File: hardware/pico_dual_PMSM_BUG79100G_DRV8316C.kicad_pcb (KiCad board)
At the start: 4 copper layers, 55 x 60 mm, 68 parts, among them IC1 BU79100G-LATR, IC2 BU79100G-LATR, IC3 BU79100G-LATR, IC4 BU79100G-LATR, IC5 THVD2450DRBR, J10 Conn_01x06, J11 Conn_01x06, J12 Conn_01x02_Pin, J2 Conn_01x02, U1 DRV8316CRRGFR, U3 DRV8316CRRGFR

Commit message: update pcb
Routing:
- net GND: vias 103 -> 104
- net (no net): vias 1 -> 0
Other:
- board text added: "LAAS CNRS tflayols 2026 OSOH"
- board text added: "M0"
- board text added: "M1"
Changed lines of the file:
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@@
 		(tags "capacitor")
 		(property "Reference" "C6"
-			(at 0 -1.16 0)
+			(at 2.05 0.05 0)
 			(layer "F.SilkS")
 			(effects
@@
 		(tags "capacitor")
 		(property "Reference" "C16"
-			(at 0 -1.16 0)
+			(at -2.4 -0.05 0)
 			(layer "F.SilkS")
 			(effects
@@
 		(tags "Integrated Circuit")
 		(property "Reference" "IC2"
-			(at 0 0 90)
+			(at 0 3.05 180)
 			(layer "F.SilkS")
 			(effects
@@
 		(tags "capacitor")
 		(property "Reference" "C8"
-			(at 0 -2.65 90)
+			(at 4.3 -0.05 90)
 			(layer "F.SilkS")
 			(effects
@@
 		(tags "resistor")
 		(property "Reference" "R20"
-			(at 0 -1.17 0)
+			(at -2.5 -0.3 0)
 			(layer "F.SilkS")
 			(effects
@@
 		(tags "capacitor")
 		(property "Reference" "C11"
-			(at 0 -1.16 0)
+			(at 2.45 0.05 0)
 			(layer "F.SilkS")
 			(effects
@@
 		(tags "Integrated Circuit")
 		(property "Reference" "IC1"
-			(at 0 0 90)
+			(at -0.1 -2.65 270)
 			(layer "F.SilkS")
 			(effects
@@
 		(tags "capacitor")
 		(property "Reference" "C5"
-			(at 0 -1.43 0)
+			(at 2.4 -0.05 0)
 			(layer "F.SilkS")
 			(effects
@@
 		(tags "capacitor")
 		(property "Reference" "C14"
-			(at 0 -1.68 0)
+			(at -0.28 -1.55 0)
 			(layer "F.SilkS")
 			(effects
@@
 		(tags "resistor")
 		(property "Reference" "R21"
-			(at 0 -1.17 0)
+			(at -2.5 -0.55 0)
 			(layer "F.SilkS")
 			(effects
@@
 			(at 0 -3.45 0)
 			(layer "F.SilkS")
+			(hide yes)
 			(effects
 				(font
@@
 		(tags "module usb pcb antenna")
 		(property "Reference" "A1"
-			(at 11.7475 24.765 270)
+			(at 6.2 -20.5375 0)
 			(unlocked yes)
 			(layer "F.SilkS")
@@
 			(at 0 -3.3 0)
 			(layer "F.SilkS")
+			(hide yes)
 			(effects
 				(font
@@
 		(tags "Integrated Circuit")
 		(property "Reference" "IC3"
-			(at 0 0 90)
+			(at 0 -2.97 180)
 			(layer "F.SilkS")
 			(effects
@@
 		(tags "resistor")
 		(property "Reference" "R14"
-			(at 0 -1.17 0)
+			(at -2.27 -0.2 0)
 			(layer "F.SilkS")
 			(effects
@@
 		(tags "resistor")
 		(property "Reference" "R13"
-			(at 0 -1.17 0)
+			(at -2.58 0.05 0)
 			(layer "F.SilkS")
 			(effects
@@
 		(tags "resistor")
 		(property "Reference" "R22"
-			(at 0 -1.17 90)
+			(at 0 -2.1 0)
 			(layer "F.SilkS")
 			(effects
@@
 		(tags "resistor")
 		(property "Reference" "R12"
-			(at 0 -1.17 0)
+			(at 0 -2.05 0)
 			(layer "F.SilkS")
 			(effects
@@
 		(tags "capacitor")
 		(property "Reference" "C21"
-			(at 0 -1.16 0)
+			(at 2.2 0.15 0)
 			(layer "F.SilkS")
 			(effects
@@
 		(tags "capacitor")
 		(property "Reference" "C12"
-			(at 0 -1.16 0)
+			(at 0.47 -1.05 0)
 			(layer "F.SilkS")
 			(effects
@@
 		(tags "resistor")
 		(property "Reference" "R23"
-			(at 0 -1.17 90)
+			(at 0 -2.1 180)
 			(layer "F.SilkS")
 			(effects
@@
 		(tags "capacitor")
 		(property "Reference" "C7"
-			(at 0 -1.16 0)
+			(at -0.13 2.5 0)
 			(layer "F.SilkS")
 			(effects
@@
 		(tags "capacitor")
 		(property "Reference" "C4"
-			(at 0 -1.16 0)
+			(at 0 -1.05 0)
 			(layer "F.SilkS")
 			(effects
@@
 		(tags "capacitor")
 		(property "Reference" "C18"
-			(at 0 -1.16 0)
+			(at -2.58 0.2 0)
 			(layer "F.SilkS")
 			(effects
@@
 		(tags "resistor")
 		(property "Reference" "R15"
-			(at 0 -1.17 0)
+			(at -2.5 -0.05 0)
 			(layer "F.SilkS")
 			(effects
@@
 		(tags "resistor")
 		(property "Reference" "R24"
-			(at 0 -1.17 0)
+			(at 0.1 1.05 0)
 			(layer "F.SilkS")
 			(effects
@@
 			(at 0 -3.45 0)
 			(layer "F.SilkS")
+			(hide yes)
 			(effects
 				(font
@@
 		(tags "resistor")
 		(property "Reference" "R19"
-			(at 0 -1.17 0)
+			(at -2.5 0.2 0)
 			(layer "F.SilkS")
 			(effects
@@
 		(tags "Integrated Circuit")
 		(property "Reference" "IC5"
-			(at 0 0 0)
+			(at -0.35 2.3 0)
 			(layer "F.SilkS")
 			(effects
@@
 		(tags "resistor")
 		(property "Reference" "R18"
-			(at 0 -1.17 0)
+			(at 2.3 0.1 0)
 			(layer "F.SilkS")
 			(effects
@@
 		(tags "resistor")
 		(property "Reference" "R26"
-			(at 0 -1.17 0)
+			(at -0.7 -0.95 0)
 			(layer "F.SilkS")
 			(effects
@@
 		(tags "capacitor")
 		(property "Reference" "C3"
-			(at 0 -1.16 0)
+			(at 0.13 -4.85 0)
 			(layer "F.SilkS")
 			(effects
@@
 			(at 0 -3.3 0)
 			(layer "F.SilkS")
+			(hide yes)
 			(effects
 				(font
@@
 		(tags "resistor")
 		(property "Reference" "R17"
-			(at 0 -1.17 0)
+			(at 0.23 -3.65 0)
 			(layer "F.SilkS")
 			(effects
@@
 		(tags "Integrated Circuit")
 		(property "Reference" "IC4"
-			(at 0 0 90)
+			(at -0.1 3.23 180)
 			(layer "F.SilkS")
 			(effects
@@
 		(tags "capacitor")
 		(property "Reference" "C20"
-			(at 0 -1.16 0)
+			(at 0.05 1.1 0)
 			(layer "F.SilkS")
 			(effects
@@
 		(tags "capacitor")
 		(property "Reference" "C25"
-			(at 0 -1.16 0)
+			(at -1.55 -1.16 0)
 			(layer "F.SilkS")
 			(effects
@@
 		(tags "connector Hirose DF13 vertical")
 		(property "Reference" "J12"
-			(at 0.62 -3.4 0)
+			(at 0.975 -3.4 0)
 			(layer "F.SilkS")
 			(effects
@@
 		(tags "capacitor")
 		(property "Reference" "C17"
-			(at 0 -1.16 0)
+			(at 0 -1.8 0)
 			(layer "F.SilkS")
 			(effects
@@
 		(tags "resistor")
 		(property "Reference" "R10"
-			(at 0 -1.17 0)
+			(at 0.05 -1.8 0)
 			(layer "F.SilkS")
 			(effects
@@
 		(tags "resistor")
 		(property "Reference" "R27"
-			(at 0 -1.17 0)
+			(at -0.05 0.8 0)
 			(layer "F.SilkS")
 			(effects
@@
 		(tags "capacitor")
 		(property "Reference" "C2"
-			(at 0 -2.65 90)
+			(at 3.58 0.29 180)
 			(layer "F.SilkS")
 			(effects
@@
 		(tags "resistor")
 		(property "Reference" "R16"
-			(at 0 -1.17 0)
+			(at -2.45 -0.2 0)
 			(layer "F.SilkS")
 			(effects
@@
 		(tags "resistor")
 		(property "Reference" "R11"
-			(at 0 -1.17 0)
+			(at -2.4 -0.2 0)
 			(layer "F.SilkS")
 			(effects
@@
 		(tags "capacitor")
 		(property "Reference" "C22"
-			(at 0 -1.68 0)
+			(at -3.1 0.2 0)
 			(layer "F.SilkS")
 			(effects
@@
 		(tags "resistor")
 		(property "Reference" "R25"
-			(at 0 -1.17 0)
+			(at -0.2 -0.95 0)
 			(layer "F.SilkS")
 			(effects
@@
 		(tags "capacitor")
 		(property "Reference" "C15"
-			(at 0 -1.16 0)
+			(at 0.05 -1.8 0)
 			(layer "F.SilkS")
 			(effects
@@
 		(tags "capacitor")
 		(property "Reference" "C1"
-			(at 0 -1.16 0)
+			(at 0.15 -1.05 0)
 			(layer "F.SilkS")
 			(effects
@@
 			(at 0 2.8 0)
 			(layer "B.SilkS")
+			(hide yes)
 			(effects
 				(font
@@
 			(at 0 2.8 0)
 			(layer "B.SilkS")
+			(hide yes)
 			(effects
 				(font
@@
 			(at 0 2.8 0)
 			(layer "B.SilkS")
+			(hide yes)
 			(effects
 				(font
@@
 			(at 0 2.8 0)
 			(layer "B.SilkS")
+			(hide yes)
 			(effects
 				(font
@@
 			(at 0 2.8 0)
 			(layer "B.SilkS")
+			(hide yes)
 			(effects
 				(font
@@
 			(at 0 2.8 0)
 			(layer "B.SilkS")
+			(hide yes)
 			(effects
 				(font
@@
 		)
 	)
+	(gr_text "M1"
+		(at 75 128 0)
+		(layer "B.SilkS")
+		(effects
+			(font
+				(size 1 1)
+				(thickness 0.1)
+			)
+			(justify left bottom mirror)
+		)
+	)
+	(gr_text "M0"
+		(at 89 128 0)
+		(layer "B.SilkS")
+		(effects
+			(font
+				(size 1 1)
+				(thickness 0.1)
+			)
+			(justify left bottom mirror)
+		)
+	)
+	(gr_text "LAAS CNRS tflayols \n2026 OSOH\n"
+		(at 110 165 0)
+		(layer "B.SilkS")
+		(effects
+			(font
+				(size 3 3)
+				(thickness 0.3)
+			)
+			(justify left bottom mirror)
+		)
+	)
 	(gr_text "U1"
 		(at 74.07 135.5 180)
@@
 		(net "")
 	)
-	(via
-		(at 77.39 131.46)
-		(size 0.6)
-		(drill 0.3)
-		(layers "F.Cu" "B.Cu")
-		(net "")
-	)
 	(segment
 		(start 76.475974 132.822033)
@@
 		(net "GND")
 	)
+	(via
+		(at 77.25 131.5)
+		(size 0.6)
+		(drill 0.3)
+		(layers "F.Cu" "B.Cu")
+		(net "GND")
+	)

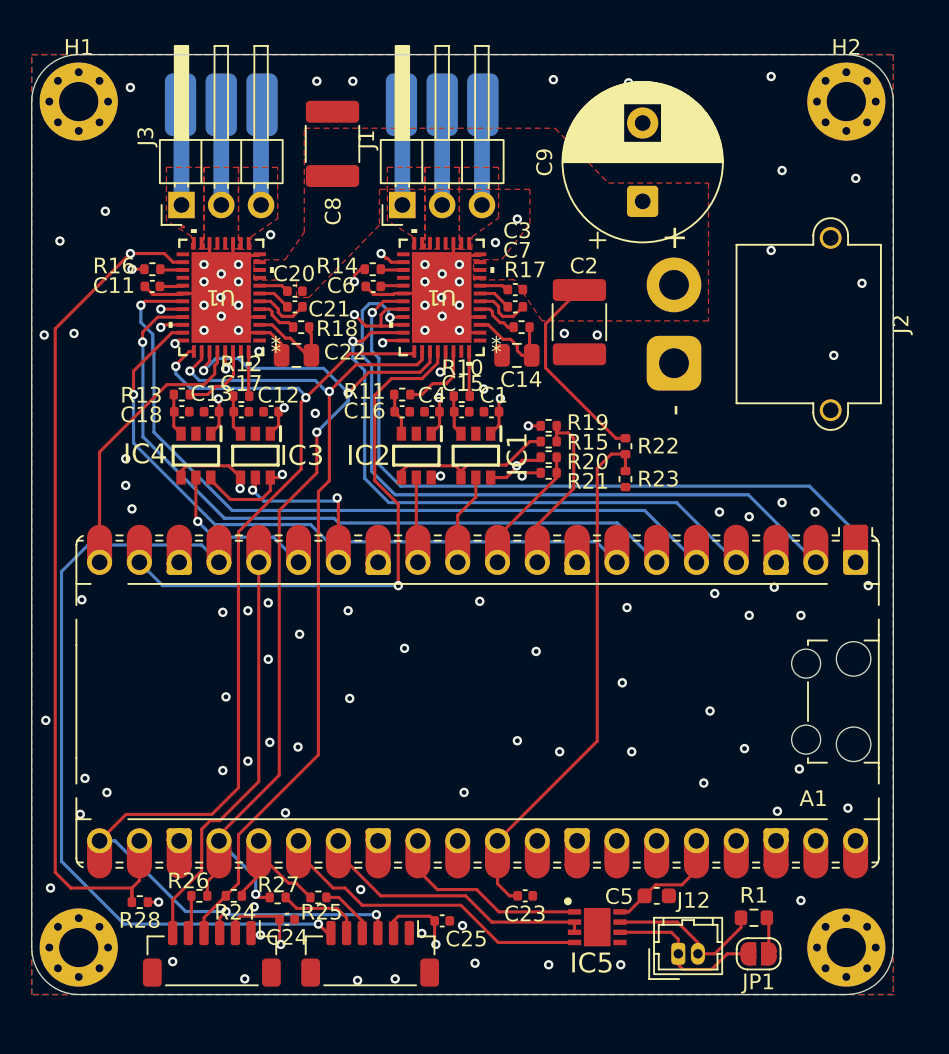
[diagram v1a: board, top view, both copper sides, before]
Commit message: add board diag at boot (press '?' at boot to test)
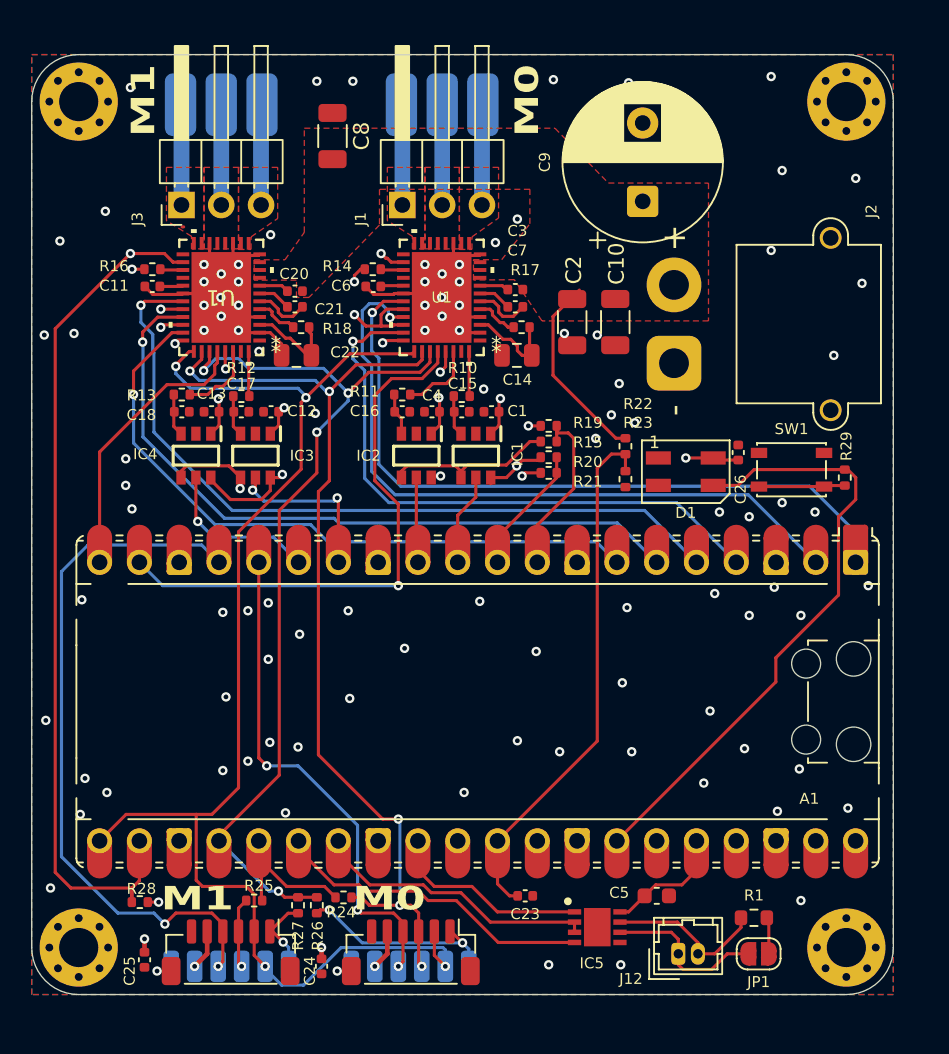
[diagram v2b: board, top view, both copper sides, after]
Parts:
- added C10: 1uF 50V, Capacitor_SMD:C_1206_3216Metric, F.Cu at (99.2, 137.1)
- added C26: 100n, Capacitor_SMD:C_0402_1005Metric, F.Cu at (107.1, 145.4)
- added D1: SK6812MINI, LED_SMD:LED_SK6812MINI_PLCC4_3.5x3.5mm_P1.75mm, F.Cu at (103.8, 146.6)
- added J14: Conn_01x01_Pin, Connector_Wire:SolderWirePad_1x01_SMD_1x2mm, B.Cu at (89.9, 178.2)
- added J15: Conn_01x01_Pin, Connector_Wire:SolderWirePad_1x01_SMD_1x2mm, B.Cu at (88.4, 178.2)
- added J16: Conn_01x01_Pin, Connector_Wire:SolderWirePad_1x01_SMD_1x2mm, B.Cu at (86.9, 178.2)
- added J17: Conn_01x01_Pin, Connector_Wire:SolderWirePad_1x01_SMD_1x2mm, B.Cu at (85.4, 178.2)
- added J18: Conn_01x01_Pin, Connector_Wire:SolderWirePad_1x01_SMD_1x2mm, B.Cu at (78.4, 178.2)
- added J19: Conn_01x01_Pin, Connector_Wire:SolderWirePad_1x01_SMD_1x2mm, B.Cu at (83.9, 178.2)
- added J20: Conn_01x01_Pin, Connector_Wire:SolderWirePad_1x01_SMD_1x2mm, B.Cu at (82.4, 178.2)
- added J21: Conn_01x01_Pin, Connector_Wire:SolderWirePad_1x01_SMD_1x2mm, B.Cu at (76.9, 178.2)
- added J22: Conn_01x01_Pin, Connector_Wire:SolderWirePad_1x01_SMD_1x2mm, B.Cu at (75.4, 178.2)
- added J23: Conn_01x01_Pin, Connector_Wire:SolderWirePad_1x01_SMD_1x2mm, B.Cu at (73.9, 178.2)
- added J24: Conn_01x01_Pin, Connector_Wire:SolderWirePad_1x01_SMD_1x2mm, B.Cu at (72.4, 178.2)
- added J25: Conn_01x01_Pin, Connector_Wire:SolderWirePad_1x01_SMD_1x2mm, B.Cu at (70.9, 178.2)
- added R29: 330, Resistor_SMD:R_0402_1005Metric, F.Cu at (113.9, 147.0)
- added SW1: PTS810SJM250SMTRLFS, Button_Switch_SMD:SW_SPST_PTS810, F.Cu at (110.5, 146.5)
- C15, C16, C17, C18: value 22p -> 100p
- C2, C8: value C -> 1uF 50V; footprint Capacitor_SMD:C_1812_4532Metric -> Capacitor_SMD:C_1206_3216Metric
- C21, C23, C24, C25, C3: value 100nF -> 100n
- C5: value C -> 100nF
- C9: value 100uF -> 100uF 50V
- J10, J11: value Conn_01x06 -> BM06B-SRSS-TB
- J12: value Conn_01x02_Pin -> DF13-02P-1.25DSA
- J2: value Conn_01x02 -> XT30PW-M
- moved C25 19.2 mm to (69.2, 177.8), turned to 90 degrees
- moved J10 12.7 mm to (86.2, 177.3)
- moved J11 8.90 mm to (74.7, 177.3)
- moved R26 7.52 mm to (80.2, 174.3), turned to 90 degrees
- moved R24 7.00 mm to (81.9, 173.8), turned to 180 degrees
- moved R25 4.10 mm to (76.2, 174.0), turned to 0 degrees
- moved C24 3.72 mm to (80.5, 178.2), turned to 90 degrees
- moved R27 1.39 mm to (79.0, 174.3), turned to 90 degrees
- moved C8 0.50 mm to (81.2, 125.2)
- moved C2 0.46 mm to (96.5, 137.1)
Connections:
- A1 pad 34: unconnected-(A1-GPIO28_ADC2-Pad34) -> /LED_SW
- J10 pad 1: GND -> /M0_ENC_CLK
- J10 pad 2: VCC -> /M0_ENC_MISO
- J10 pad 3: /M0_ENC_MISO -> /M0_ENC_MOSI
- J10 pad 4: /M0_ENC_MOSI -> /M0_ENC_CS
- J10 pad 5: /M0_ENC_CLK -> VCC
- J10 pad 6: /M0_ENC_CS -> GND
- J11 pad 1: GND -> /M1_ENC_CLK
- J11 pad 2: VCC -> /M0_ENC_MISO
- J11 pad 3: /M0_ENC_MISO -> /M1_ENC_MOSI
- J11 pad 4: /M1_ENC_MOSI -> /M1_ENC_CS
- J11 pad 5: /M1_ENC_CLK -> VCC
- J11 pad 6: /M1_ENC_CS -> GND
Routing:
- net VCC: track 168.9 -> 210.2 mm, vias 16 -> 19
- net /LED_SW: track 0.00 -> 38.7 mm
- net /M0_ENC_CLK: track 2.45 -> 13.0 mm, vias 0 -> 2
- net /M0_ENC_MISO: track 78.5 -> 86.0 mm
- net /M0_ENC_MOSI: track 56.2 -> 62.3 mm, vias 2 -> 5
- net Net-(R29-Pad2): track 0.00 -> 6.00 mm
- net /M0_ENC_CS: track 26.3 -> 32.1 mm, vias 0 -> 3
- net /SPI0_MOSI: track 7.62 -> 11.6 mm
- net /M1_ENC_CS: track 48.8 -> 44.9 mm, vias 1 -> 2
- net /M1_ENC_MOSI: track 3.69 -> 4.49 mm, vias 0 -> 1
- net /M1_ENC_CLK: track 5.40 -> 5.11 mm, vias 0 -> 1
- net GND: vias 104 -> 100
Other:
- board text added: "GND VCC CS MOSI MISO SCK"
- board text added: "SCK MISO MOSI CS VCC GND"
